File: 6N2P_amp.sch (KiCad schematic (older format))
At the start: 78 parts, among them J1 guitar_in, J2 speaker, J3 fx_send, J4 fx_return, U1 ECC83, U2 ECC83, U3 6N1P, U4 DSN-MINI-360, U5 DSN-MINI-360, U6 DSN-MINI-360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

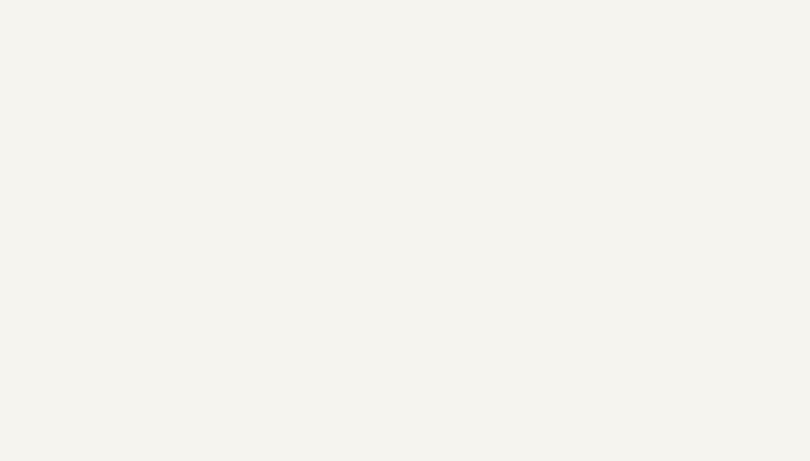
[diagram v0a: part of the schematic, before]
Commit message: introduced foot switch jack
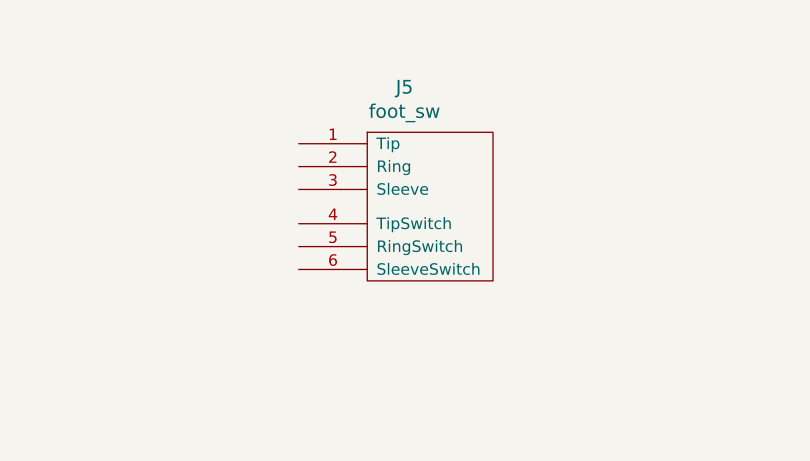
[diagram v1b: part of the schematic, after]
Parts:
- added J5: foot_sw, micha_custom:Reichelt_EBS63P, symbol micha_custom:6.3MMTRSSwitched
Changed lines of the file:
@@
 Text Notes 1550 13600 0    118  ~ 0
 TODO:\nLDR footprints are too big\nfootswitch -> 2n7000 inverter to swith CL and OD nets
+$Comp
+L micha_custom:6.3MMTRSSwitched J5
+U 1 1 5F86FF44
+P 9150 2050
+F 0 "J5" H 9113 2197 60  0000 C CNN
+F 1 "foot_sw" H 9113 2091 60  0000 C CNN
+F 2 "micha_custom:Reichelt_EBS63P" H 9150 2050 60  0001 C CNN
+F 3 "" H 9150 2050 60  0000 C CNN
+	1    9150 2050
+	1    0    0    -1
+$EndComp
 $EndSCHEMATC

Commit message: genug fuer heute
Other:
- note added: "TODO:\nLDR footprints are too big\nfootswitch -> 2n7000 inverter to swith CL and OD nets\nLDRs before the tone stack?"
- note removed: "TODO:\nLDR footprints are too big\nfootswitch -> 2n7000 inverter to swith CL and OD nets"
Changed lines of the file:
@@
 	12900 8500 12900 8450
 Text Notes 1550 13600 0    118  ~ 0
-TODO:\nLDR footprints are too big\nfootswitch -> 2n7000 inverter to swith CL and OD nets
+TODO:\nLDR footprints are too big\nfootswitch -> 2n7000 inverter to swith CL and OD nets\nLDRs before the tone stack?
 $Comp
 L micha_custom:6.3MMTRSSwitched J5

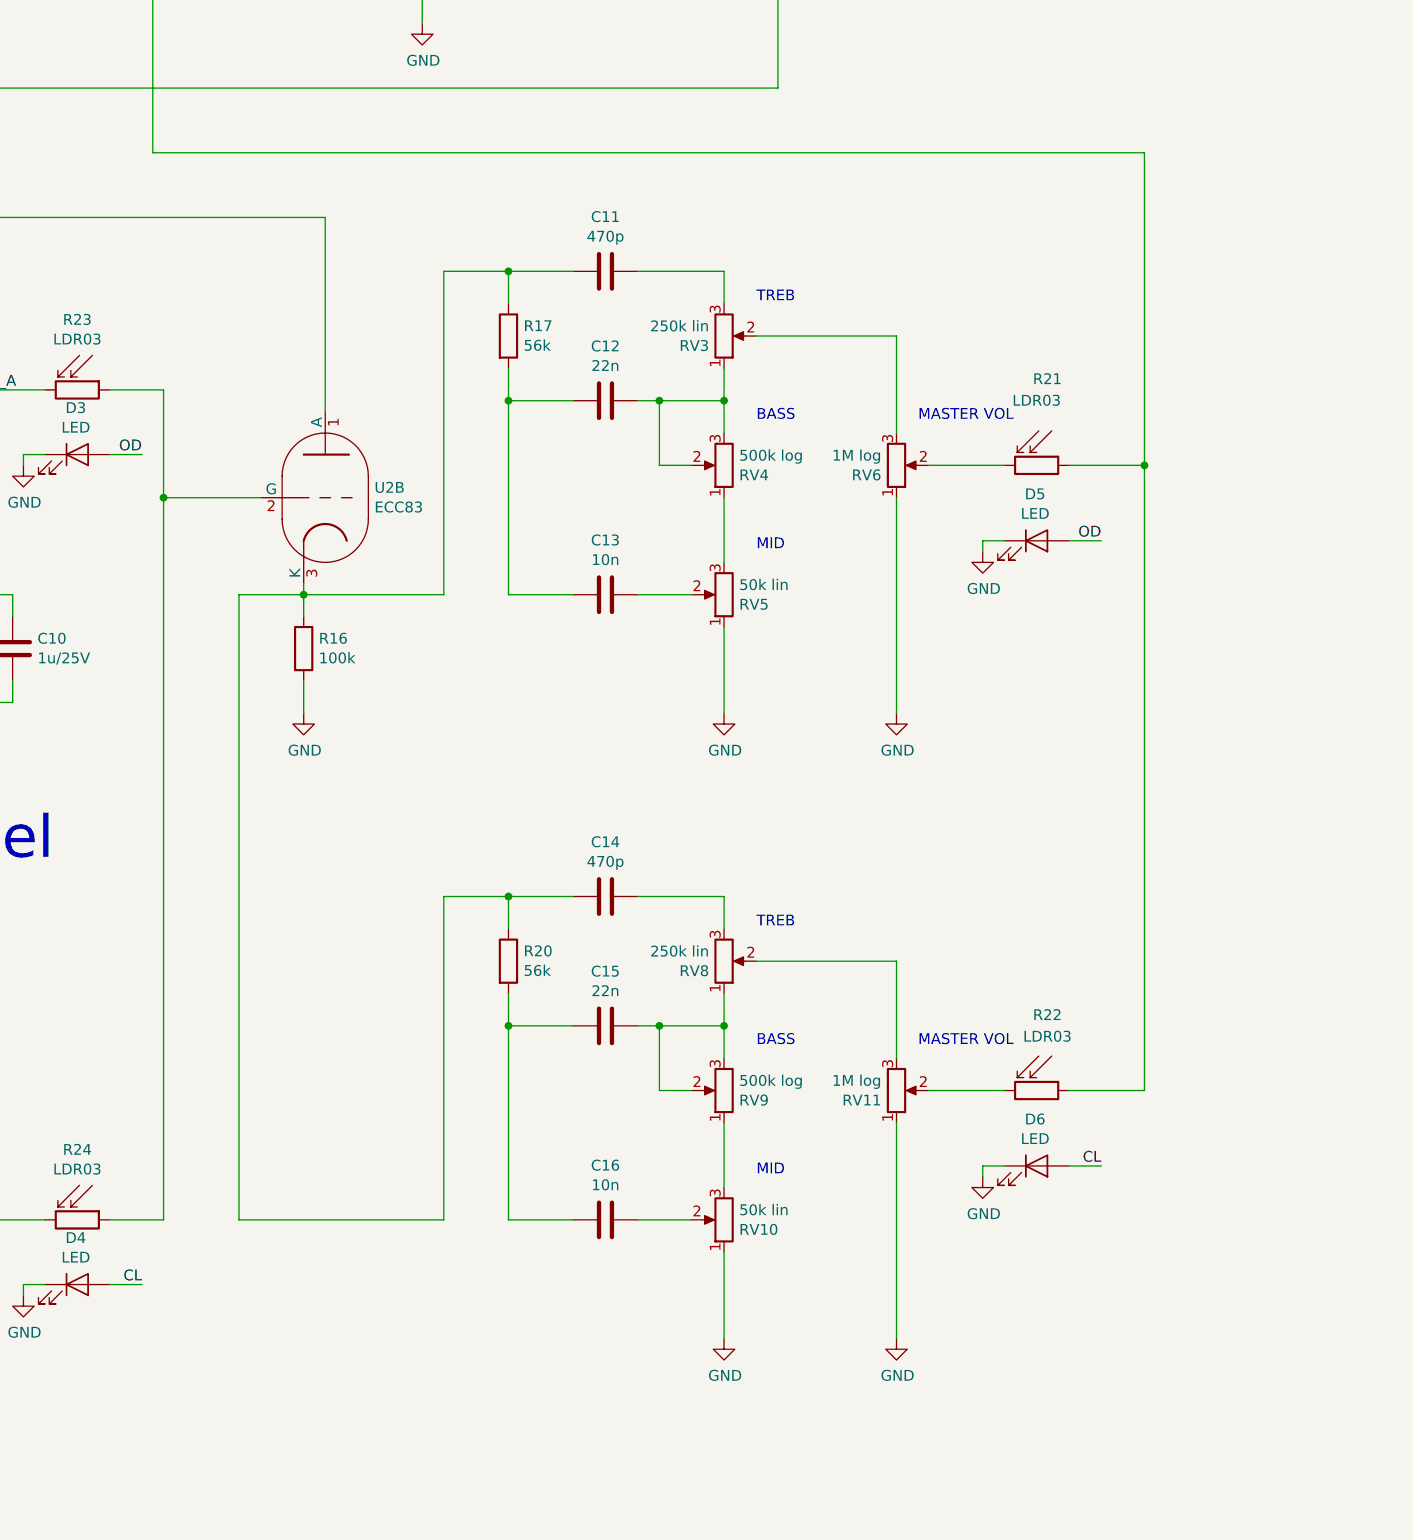
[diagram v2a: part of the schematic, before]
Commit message: more LDRs
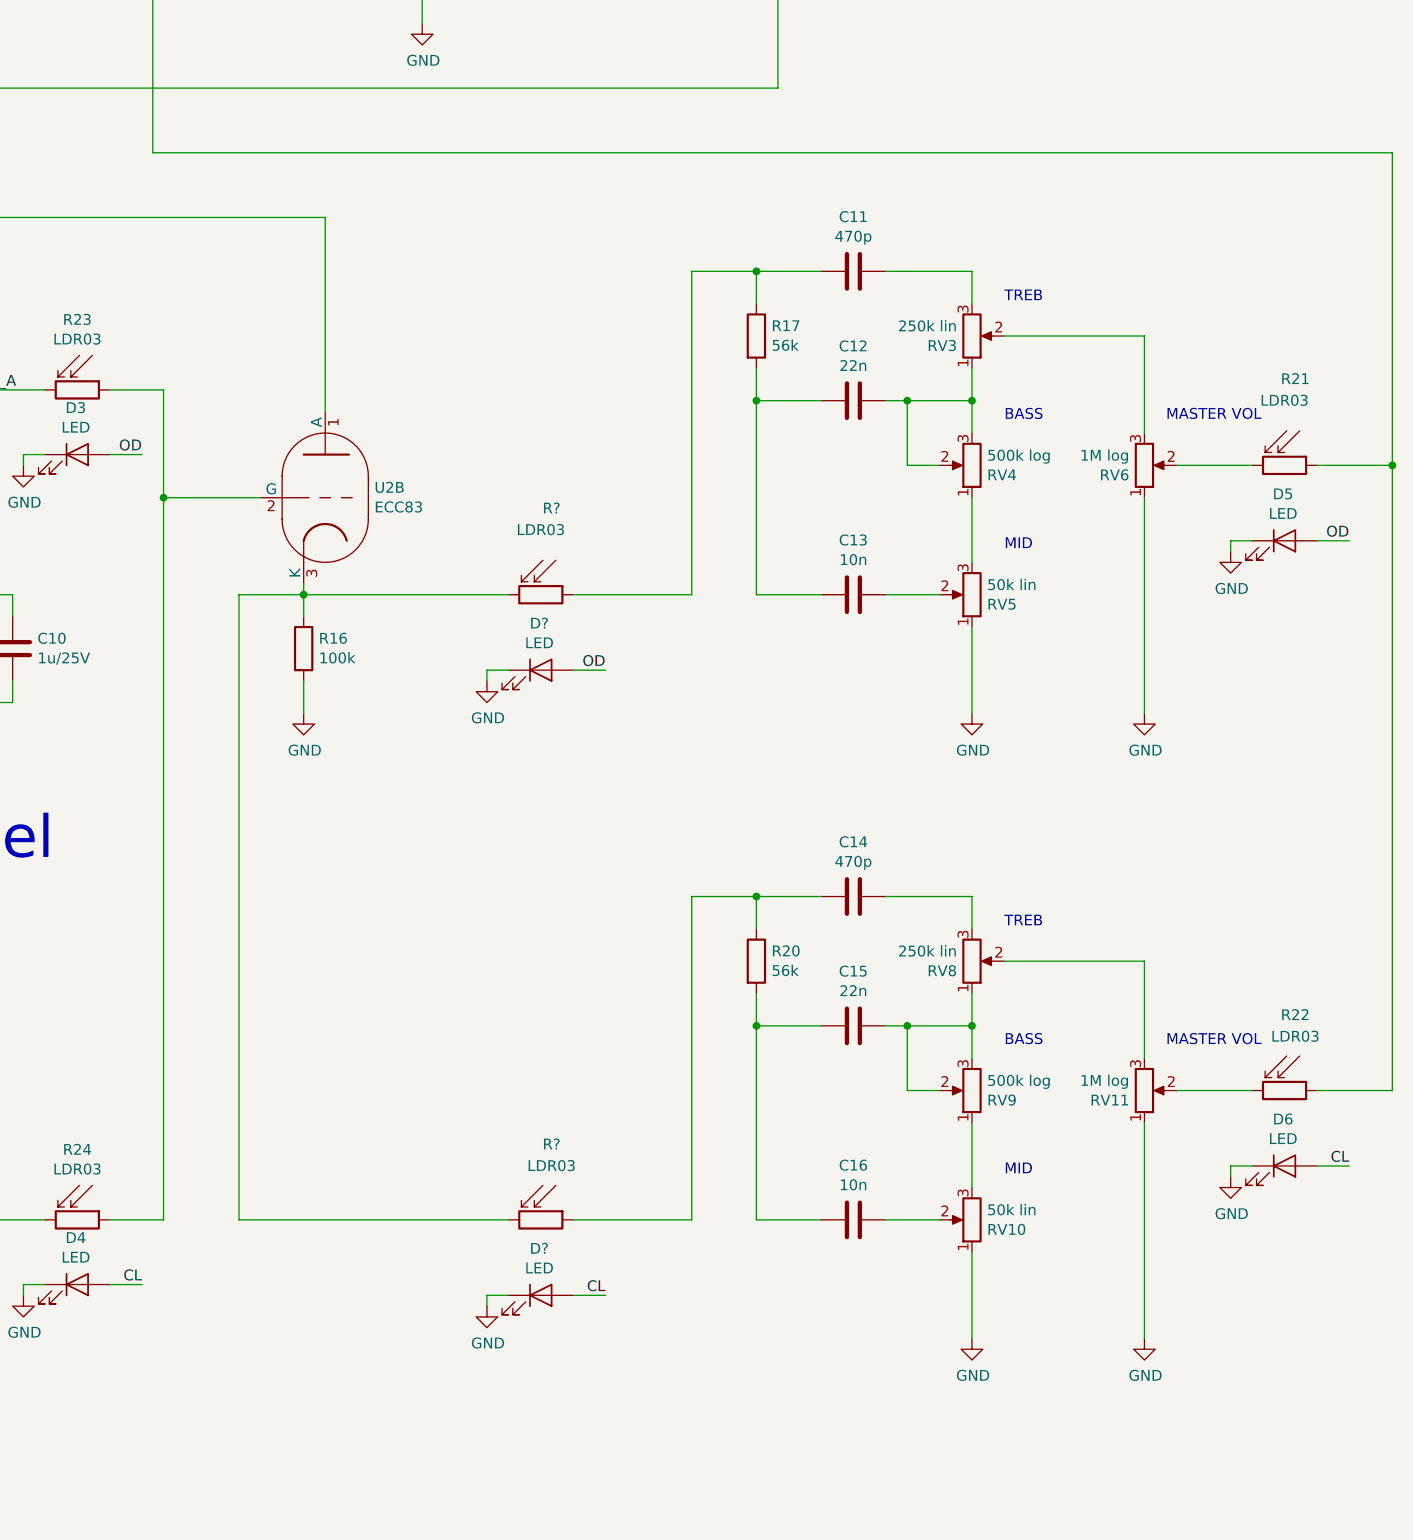
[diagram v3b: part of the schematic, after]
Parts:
- added D? (x2): LED, LED_THT:LED_D5.0mm, symbol Device:LED
- added R? (x2): LDR03, OptoDevice:R_LDR_4.9x4.2mm_P2.54mm_Vertical, symbol Sensor_Optical:LDR03
- R18, R19, R21, R22, R23, R24: footprint OptoDevice:R_LDR_10x8.5mm_P7.6mm_Vertical -> OptoDevice:R_LDR_4.9x4.2mm_P2.54mm_Vertical
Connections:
- net CL: now also D?.2 (A)
- net GND: now also D?.1 (K), D?.1 (K)
- net OD: now also D?.2 (A)
- new net: R16.1, R?.2, R?.2, U2.3 (K)
- new net: C11.2, R17.1, R?.1
- new net: C14.2, R20.1, R?.1
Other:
- moved on the sheet: C11, C12, C13, C14, C15, C16, D5, D6, R17, R20, R21, R22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

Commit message: LDRs
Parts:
- gave numbers to parts that had none: 4
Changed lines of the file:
@@
 	13500 7050 19250 7050
 $Comp
-L Sensor_Optical:LDR03 R?
+L Sensor_Optical:LDR03 R34
 U 1 1 5F5579F1
 P 15300 9100
-F 0 "R?" V 14900 9150 50  0000 C CNN
+F 0 "R34" V 14900 9150 50  0000 C CNN
 F 1 "LDR03" V 15000 9100 50  0000 C CNN
 F 2 "OptoDevice:R_LDR_4.9x4.2mm_P2.54mm_Vertical" V 15475 9100 50  0001 C CNN
@@
 $EndComp
 $Comp
-L Device:LED D?
+L Device:LED D7
 U 1 1 5F5579FC
 P 15300 9450
-F 0 "D?" H 15293 9666 50  0000 C CNN
+F 0 "D7" H 15293 9666 50  0000 C CNN
 F 1 "LED" H 15293 9575 50  0000 C CNN
 F 2 "LED_THT:LED_D5.0mm" H 15300 9450 50  0001 C CNN
@@
 $EndComp
 $Comp
-L power:GND #PWR?
+L power:GND #PWR039
 U 1 1 5F557A06
 P 15050 9500
-F 0 "#PWR?" H 15050 9250 50  0001 C CNN
+F 0 "#PWR039" H 15050 9250 50  0001 C CNN
 F 1 "GND" H 15055 9327 50  0000 C CNN
 F 2 "" H 15050 9500 50  0001 C CNN
@@
 	14200 9100 15150 9100
 $Comp
-L Sensor_Optical:LDR03 R?
+L Sensor_Optical:LDR03 R35
 U 1 1 5F5837AA
 P 15300 12000
-F 0 "R?" V 14950 12050 50  0000 C CNN
+F 0 "R35" V 14950 12050 50  0000 C CNN
 F 1 "LDR03" V 15050 12050 50  0000 C CNN
 F 2 "OptoDevice:R_LDR_4.9x4.2mm_P2.54mm_Vertical" V 15475 12000 50  0001 C CNN
@@
 $EndComp
 $Comp
-L Device:LED D?
+L Device:LED D8
 U 1 1 5F5837B5
 P 15300 12350
-F 0 "D?" H 15293 12566 50  0000 C CNN
+F 0 "D8" H 15293 12566 50  0000 C CNN
 F 1 "LED" H 15293 12475 50  0000 C CNN
 F 2 "LED_THT:LED_D5.0mm" H 15300 12350 50  0001 C CNN
@@
 $EndComp
 $Comp
-L power:GND #PWR?
+L power:GND #PWR040
 U 1 1 5F5837BF
 P 15050 12400
-F 0 "#PWR?" H 15050 12150 50  0001 C CNN
+F 0 "#PWR040" H 15050 12150 50  0001 C CNN
 F 1 "GND" H 15055 12227 50  0000 C CNN
 F 2 "" H 15050 12400 50  0001 C CNN

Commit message: snap
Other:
- note added: "TODO:\n\nfootswitch -> 2n7000 inverter to swith CL and OD nets\npower input hohlstecker pcb"
- note removed: "TODO:\nLDR footprints are too big\nfootswitch -> 2n7000 inverter to swith CL and OD nets\nLDRs before the tone stack?"
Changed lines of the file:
@@
 	12900 8500 12900 8450
 Text Notes 1550 13600 0    118  ~ 0
-TODO:\nLDR footprints are too big\nfootswitch -> 2n7000 inverter to swith CL and OD nets\nLDRs before the tone stack?
+TODO:\n\nfootswitch -> 2n7000 inverter to swith CL and OD nets\npower input hohlstecker pcb
 $Comp
 L micha_custom:6.3MMTRSSwitched J5

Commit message: snap
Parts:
- RV1, RV2, RV3, RV4, RV5, RV6: footprint Potentiometer_THT:Potentiometer_Alps_RK163_Single_Horizontal -> Connector_PinHeader_2.54mm:PinHeader_1x03_P2.54mm_Vertical
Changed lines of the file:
@@
 F 0 "RV1" H 7430 9096 50  0000 R CNN
 F 1 "500k log" H 7430 9005 50  0000 R CNN
-F 2 "Potentiometer_THT:Potentiometer_Alps_RK163_Single_Horizontal" H 7500 9050 50  0001 C CNN
+F 2 "Connector_PinHeader_2.54mm:PinHeader_1x03_P2.54mm_Vertical" H 7500 9050 50  0001 C CNN
 F 3 "~" H 7500 9050 50  0001 C CNN
 	1    7500 9050
@@
 F 0 "RV2" H 10780 9096 50  0000 R CNN
 F 1 "500k log" H 10780 9005 50  0000 R CNN
-F 2 "Potentiometer_THT:Potentiometer_Alps_RK163_Single_Horizontal" H 10850 9050 50  0001 C CNN
+F 2 "Connector_PinHeader_2.54mm:PinHeader_1x03_P2.54mm_Vertical" H 10850 9050 50  0001 C CNN
 F 3 "~" H 10850 9050 50  0001 C CNN
 	1    10850 9050
@@
 F 0 "RV5" H 17230 9146 50  0000 R CNN
 F 1 "50k lin" H 17230 9055 50  0000 R CNN
-F 2 "Potentiometer_THT:Potentiometer_Alps_RK163_Single_Horizontal" H 17300 9100 50  0001 C CNN
+F 2 "Connector_PinHeader_2.54mm:PinHeader_1x03_P2.54mm_Vertical" H 17300 9100 50  0001 C CNN
 F 3 "~" H 17300 9100 50  0001 C CNN
 	1    17300 9100
@@
 F 0 "RV4" H 17230 8546 50  0000 R CNN
 F 1 "500k log" H 17230 8455 50  0000 R CNN
-F 2 "Potentiometer_THT:Potentiometer_Alps_RK163_Single_Horizontal" H 17300 8500 50  0001 C CNN
+F 2 "Connector_PinHeader_2.54mm:PinHeader_1x03_P2.54mm_Vertical" H 17300 8500 50  0001 C CNN
 F 3 "~" H 17300 8500 50  0001 C CNN
 	1    17300 8500
@@
 F 0 "RV3" H 17231 7946 50  0000 R CNN
 F 1 "250k lin" H 17231 7855 50  0000 R CNN
-F 2 "Potentiometer_THT:Potentiometer_Alps_RK163_Single_Horizontal" H 17300 7900 50  0001 C CNN
+F 2 "Connector_PinHeader_2.54mm:PinHeader_1x03_P2.54mm_Vertical" H 17300 7900 50  0001 C CNN
 F 3 "~" H 17300 7900 50  0001 C CNN
 	1    17300 7900
@@
 F 0 "RV6" H 18030 8546 50  0000 R CNN
 F 1 "1M log" H 18030 8455 50  0000 R CNN
-F 2 "Potentiometer_THT:Potentiometer_Alps_RK163_Single_Horizontal" H 18100 8500 50  0001 C CNN
+F 2 "Connector_PinHeader_2.54mm:PinHeader_1x03_P2.54mm_Vertical" H 18100 8500 50  0001 C CNN
 F 3 "~" H 18100 8500 50  0001 C CNN
 	1    18100 8500

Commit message: new evening
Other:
- note added: "TODO:\n\nfootswitch -> 2n7000 inverter to swith CL and OD nets\npower input hohlstecker pcb\n\n470R resistors for LEDs\n25mm space between LDR and LED"
- note removed: "TODO:\n\nfootswitch -> 2n7000 inverter to swith CL and OD nets\npower input hohlstecker pcb"
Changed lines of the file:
@@
 	12900 8500 12900 8450
 Text Notes 1550 13600 0    118  ~ 0
-TODO:\n\nfootswitch -> 2n7000 inverter to swith CL and OD nets\npower input hohlstecker pcb
+TODO:\n\nfootswitch -> 2n7000 inverter to swith CL and OD nets\npower input hohlstecker pcb\n\n470R resistors for LEDs\n25mm space between LDR and LED
 $Comp
 L micha_custom:6.3MMTRSSwitched J5

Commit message: we have resistors now for the LEDs
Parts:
- added R36, R37, R38, R39, R40, R41, R42, R43: 470, Resistor_THT:R_Axial_DIN0309_L9.0mm_D3.2mm_P2.54mm_Vertical, symbol Device:R
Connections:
- net CL: now also R37.1, R39.1, R41.1, R43.1; no longer D2.2 (A), D4.2 (A), D6.2 (A), D8.2 (A)
- net OD: now also R36.1, R38.1, R40.1, R42.1; no longer D1.2 (A), D3.2 (A), D5.2 (A), D7.2 (A)
- new net: D2.2 (A), R37.2
- new net: D1.2 (A), R36.2
- new net: D7.2 (A), R40.2
- new net: D5.2 (A), R42.2
- new net: D8.2 (A), R41.2
- new net: D4.2 (A), R39.2
- new net: D6.2 (A), R43.2
- new net: D3.2 (A), R38.2
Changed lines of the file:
@@
 Wire Wire Line
 	8100 9400 8250 9400
-Text Label 8250 9400 2    50   ~ 0
-OD
 $Comp
 L Device:LED D2
@@
 Wire Wire Line
 	8100 12300 8250 12300
-Text Label 8250 12300 2    50   ~ 0
+Text Label 8000 12700 0    50   ~ 0
 CL
 $Comp
@@
 Wire Wire Line
 	13300 12300 13450 12300
-Text Label 13450 12300 2    50   ~ 0
-CL
 $Comp
 L Device:LED D6
@@
 Wire Wire Line
 	18900 11750 19050 11750
-Text Label 19050 11750 2    50   ~ 0
-CL
 $Comp
 L Device:LED D5
@@
 Wire Wire Line
 	18900 8850 19050 8850
-Text Label 19050 8850 2    50   ~ 0
-OD
 Wire Wire Line
 	18500 8900 18500 8850
@@
 Wire Wire Line
 	13300 8450 13450 8450
-Text Label 13450 8450 2    50   ~ 0
-OD
 Wire Wire Line
 	12900 8500 12900 8450
@@
 Wire Wire Line
 	15450 9450 15600 9450
-Text Label 15600 9450 2    50   ~ 0
-OD
 Wire Wire Line
 	15050 9500 15050 9450
@@
 Wire Wire Line
 	15450 12350 15600 12350
-Text Label 15600 12350 2    50   ~ 0
+Wire Wire Line
+	15450 12000 16000 12000
+Wire Wire Line
+	13900 12000 15150 12000
+$Comp
+L Device:R R37
+U 1 1 5F4D054F
+P 8250 12500
+F 0 "R37" V 8450 12500 50  0000 C CNN
+F 1 "470" V 8350 12500 50  0000 C CNN
+F 2 "Resistor_THT:R_Axial_DIN0309_L9.0mm_D3.2mm_P2.54mm_Vertical" V 8180 12500 50  0001 C CNN
+F 3 "~" H 8250 12500 50  0001 C CNN
+	1    8250 12500
+	-1   0    0    1
+$EndComp
+Wire Wire Line
+	8250 12300 8250 12350
+Wire Wire Line
+	8250 12650 8250 12700
+Wire Wire Line
+	8250 12700 8000 12700
+Text Label 8000 9800 0    50   ~ 0
+OD
+$Comp
+L Device:R R36
+U 1 1 5F50E6B5
+P 8250 9600
+F 0 "R36" V 8450 9600 50  0000 C CNN
+F 1 "470" V 8350 9600 50  0000 C CNN
+F 2 "Resistor_THT:R_Axial_DIN0309_L9.0mm_D3.2mm_P2.54mm_Vertical" V 8180 9600 50  0001 C CNN
+F 3 "~" H 8250 9600 50  0001 C CNN
+	1    8250 9600
+	-1   0    0    1
+$EndComp
+Wire Wire Line
+	8250 9400 8250 9450
+Wire Wire Line
+	8250 9750 8250 9800
+Wire Wire Line
+	8250 9800 8000 9800
+Text Label 18800 9250 0    50   ~ 0
+OD
+$Comp
+L Device:R R42
+U 1 1 5F57AD8C
+P 19050 9050
+F 0 "R42" V 19250 9050 50  0000 C CNN
+F 1 "470" V 19150 9050 50  0000 C CNN
+F 2 "Resistor_THT:R_Axial_DIN0309_L9.0mm_D3.2mm_P2.54mm_Vertical" V 18980 9050 50  0001 C CNN
+F 3 "~" H 19050 9050 50  0001 C CNN
+	1    19050 9050
+	-1   0    0    1
+$EndComp
+Wire Wire Line
+	19050 8850 19050 8900
+Wire Wire Line
+	19050 9200 19050 9250
+Wire Wire Line
+	19050 9250 18800 9250
+Text Label 13200 12700 0    50   ~ 0
 CL
-Wire Wire Line
-	15450 12000 16000 12000
-Wire Wire Line
-	13900 12000 15150 12000
+$Comp
+L Device:R R39
+U 1 1 5F5C152F
+P 13450 12500
+F 0 "R39" V 13650 12500 50  0000 C CNN
+F 1 "470" V 13550 12500 50  0000 C CNN
+F 2 "Resistor_THT:R_Axial_DIN0309_L9.0mm_D3.2mm_P2.54mm_Vertical" V 13380 12500 50  0001 C CNN
+F 3 "~" H 13450 12500 50  0001 C CNN
+	1    13450 12500
+	-1   0    0    1
+$EndComp
+Wire Wire Line
+	13450 12300 13450 12350
+Wire Wire Line
+	13450 12650 13450 12700
+Wire Wire Line
+	13450 12700 13200 12700
+Text Label 15350 12750 0    50   ~ 0
+CL
+$Comp
+L Device:R R41
+U 1 1 5F5E0D3C
+P 15600 12550
+F 0 "R41" V 15800 12550 50  0000 C CNN
+F 1 "470" V 15700 12550 50  0000 C CNN
+F 2 "Resistor_THT:R_Axial_DIN0309_L9.0mm_D3.2mm_P2.54mm_Vertical" V 15530 12550 50  0001 C CNN
+F 3 "~" H 15600 12550 50  0001 C CNN
+	1    15600 12550
+	-1   0    0    1
+$EndComp
+Wire Wire Line
+	15600 12350 15600 12400
+Wire Wire Line
+	15600 12700 15600 12750
+Wire Wire Line
+	15600 12750 15350 12750
+Text Label 18800 12150 0    50   ~ 0
+CL
+$Comp
+L Device:R R43
+U 1 1 5F604CE4
+P 19050 11950
+F 0 "R43" V 19250 11950 50  0000 C CNN
+F 1 "470" V 19150 11950 50  0000 C CNN
+F 2 "Resistor_THT:R_Axial_DIN0309_L9.0mm_D3.2mm_P2.54mm_Vertical" V 18980 11950 50  0001 C CNN
+F 3 "~" H 19050 11950 50  0001 C CNN
+	1    19050 11950
+	-1   0    0    1
+$EndComp
+Wire Wire Line
+	19050 11750 19050 11800
+Wire Wire Line
+	19050 12100 19050 12150
+Wire Wire Line
+	19050 12150 18800 12150
+Text Label 13200 8850 0    50   ~ 0
+OD
+$Comp
+L Device:R R38
+U 1 1 5F6359B9
+P 13450 8650
+F 0 "R38" V 13650 8650 50  0000 C CNN
+F 1 "470" V 13550 8650 50  0000 C CNN
+F 2 "Resistor_THT:R_Axial_DIN0309_L9.0mm_D3.2mm_P2.54mm_Vertical" V 13380 8650 50  0001 C CNN
+F 3 "~" H 13450 8650 50  0001 C CNN
+	1    13450 8650
+	-1   0    0    1
+$EndComp
+Wire Wire Line
+	13450 8450 13450 8500
+Wire Wire Line
+	13450 8800 13450 8850
+Wire Wire Line
+	13450 8850 13200 8850
+Text Label 15350 9850 0    50   ~ 0
+OD
+$Comp
+L Device:R R40
+U 1 1 5F667707
+P 15600 9650
+F 0 "R40" V 15800 9650 50  0000 C CNN
+F 1 "470" V 15700 9650 50  0000 C CNN
+F 2 "Resistor_THT:R_Axial_DIN0309_L9.0mm_D3.2mm_P2.54mm_Vertical" V 15530 9650 50  0001 C CNN
+F 3 "~" H 15600 9650 50  0001 C CNN
+	1    15600 9650
+	-1   0    0    1
+$EndComp
+Wire Wire Line
+	15600 9450 15600 9500
+Wire Wire Line
+	15600 9800 15600 9850
+Wire Wire Line
+	15600 9850 15350 9850
 $EndSCHEMATC
